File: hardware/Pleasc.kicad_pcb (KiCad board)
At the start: 4 copper layers, 60 x 60 mm, 96 parts, among them J1 2601-1104, J3 ESQ-110-14-G-D, J4 2601-1104, J5 XT30PW-M, Q1 AO3400A, Q10 AO3400A, Q11 AO3400A, Q12 AO3400A, Q13 AO3400A, Q14 AO3400A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

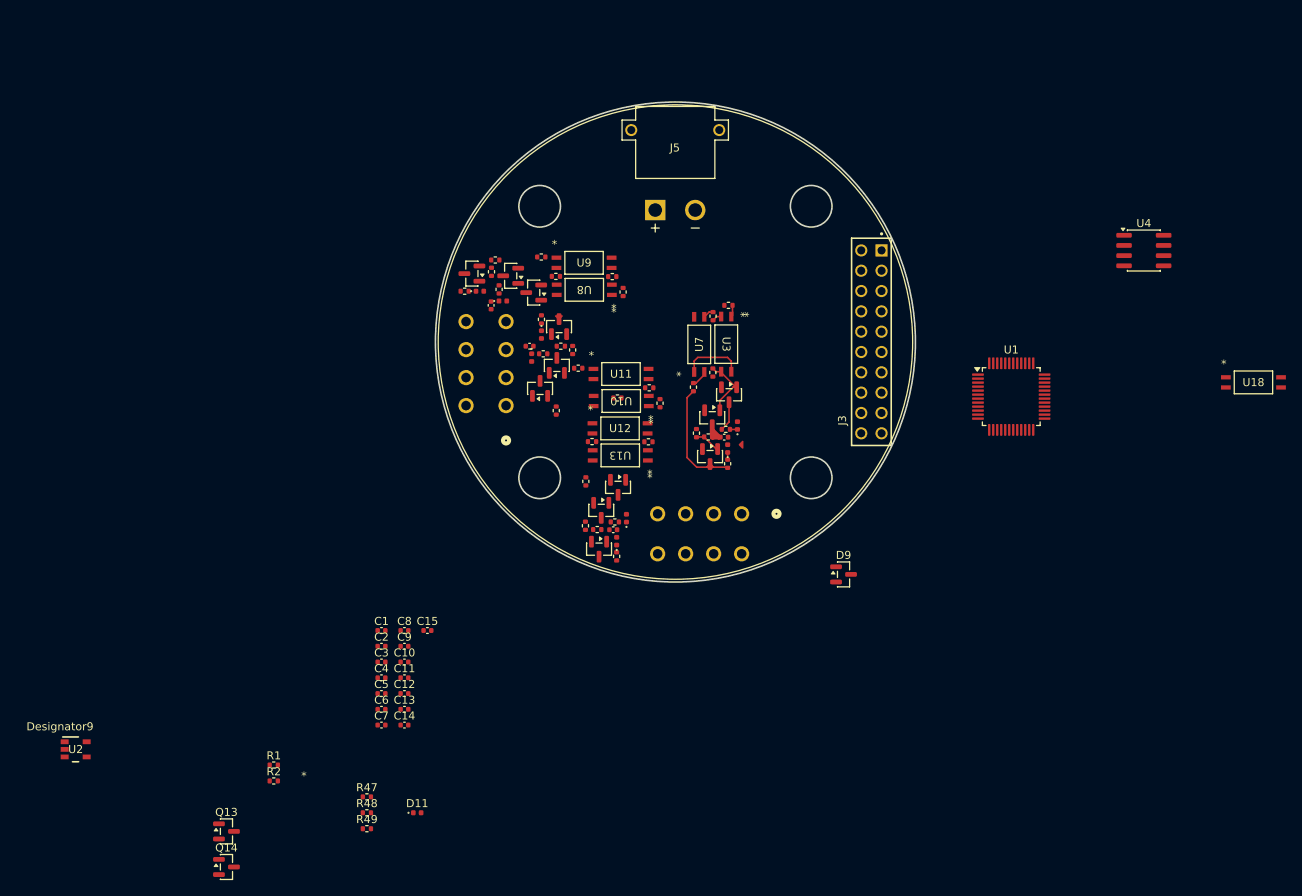
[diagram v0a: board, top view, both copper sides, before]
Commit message: Schematic complete, components layed out on the PCB
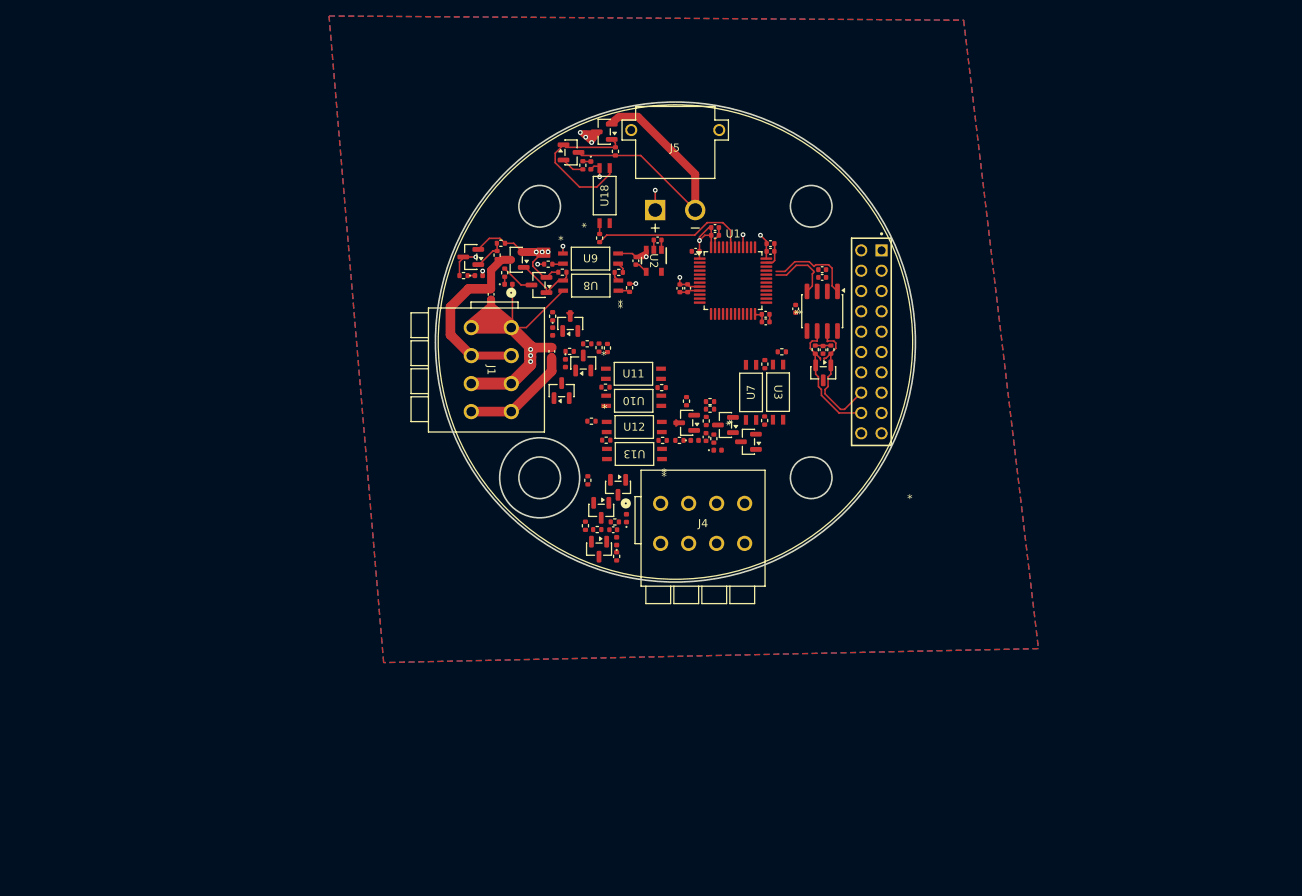
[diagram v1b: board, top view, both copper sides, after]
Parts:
- J1, J4: moved to F.Cu
- moved Q14 103.3 mm to (180.6, 60.5), turned to 180 degrees
- moved Q13 95.2 mm to (176.4, 63.0)
- moved U2 94.6 mm to (186.8, 76.6), turned to -90 degrees
- moved R48 88.3 mm to (181.9, 62.9), turned to -90 degrees
- moved R2 88.1 mm to (208.9, 87.7), turned to 90 degrees
- moved R49 87.2 mm to (177.9, 64.6), turned to 90 degrees
- moved R1 85.3 mm to (206.9, 87.7), turned to -90 degrees
- moved U18 84.4 mm to (180.6, 68.4), turned to 90 degrees
- moved D11 83.8 mm to (178.9, 64.7), turned to -90 degrees
- moved R47 75.7 mm to (180.0, 73.7), turned to 90 degrees
- moved C13 75.1 mm to (207.8, 78.7)
- moved C12 74.4 mm to (207.8, 77.7)
- moved C14 71.4 mm to (204.5, 82.6), turned to 90 degrees
- moved C3 67.7 mm to (194.4, 73.4)
- moved C9 67.3 mm to (201.3, 75.4)
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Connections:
- D11 pad 1: Net-(D11-K) -> unconnected-(D11-K-Pad1)
- J1 pad 3: /Aux1 neg -> /Main neg
- J1 pad 4: /Aux1 neg -> /Main neg
- J1 pad 7: /Aux2 neg -> /Aux1 neg
- J1 pad 8: /Aux2 neg -> /Aux1 neg
- J4 pad 7: /Main neg -> /Aux2 neg
- J4 pad 8: /Main neg -> /Aux2 neg
- Q1 pad 1: /Drogue neg -> Net-(Q1-G)
- Q10 pad 1: /Aux2 neg -> Net-(Q10-G)
- Q11 pad 1: /Aux2 neg -> Net-(Q10-G)
- Q13 pad 1: Net-(D11-K) -> Net-(Q13-G)
- Q14 pad 1: Net-(D11-K) -> Net-(Q13-G)
- Q2 pad 1: /Drogue neg -> Net-(Q1-G)
- Q4 pad 1: /Main neg -> Net-(Q4-G)
- Q5 pad 1: /Main neg -> Net-(Q4-G)
- Q7 pad 1: /Aux1 neg -> Net-(Q7-G)
- Q8 pad 1: /Aux1 neg -> Net-(Q7-G)
- R16 pad 1: /Main neg -> Net-(Q4-G)
- R25 pad 1: /Aux1 neg -> Net-(Q7-G)
- R34 pad 1: /Aux2 neg -> Net-(Q10-G)
- R48 pad 1: Net-(D11-K) -> Net-(Q13-G)
- R49 pad 2: Net-(D11-K) -> unconnected-(D11-K-Pad1)
- R6 pad 1: /Drogue neg -> Net-(Q1-G)
- U10 pad 3: /Aux1 neg -> Net-(Q7-G)
- U12 pad 3: /Aux2 neg -> Net-(Q10-G)
- U18 pad 3: Net-(D11-K) -> Net-(Q13-G)
- U3 pad 3: /Drogue neg -> Net-(Q1-G)
- U8 pad 3: /Main neg -> Net-(Q4-G)
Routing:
- net VBAT_AUX1: track 7.71 -> 95.3 mm, vias 0 -> 7
- net Net-(Q13-D): track 0.00 -> 34.5 mm
- net PGND: track 0.00 -> 34.2 mm, vias 0 -> 6
- net /Main neg: track 0.00 -> 23.5 mm
- net 3.3V: track 0.00 -> 21.2 mm, vias 0 -> 3
- net Net-(Q13-G): track 0.00 -> 20.4 mm
- net PYRO_ON: track 0.00 -> 19.5 mm
- net MAIN_FIRE: track 0.00 -> 18.3 mm, vias 0 -> 2
- net CAN_o+: track 0.00 -> 16.9 mm
- net CAN_o-: track 0.00 -> 16.3 mm
- net Net-(Q3-D): track 14.5 -> 0.00 mm
- net /Aux1 neg: track 0.00 -> 13.8 mm
- net GND: track 1.20 -> 14.5 mm, vias 0 -> 1
- net Net-(Q6-D): track 0.00 -> 12.9 mm, vias 0 -> 2
- net /Drogue neg: track 12.2 -> 0.00 mm
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- added copper zone on B.Cu, net GND
- added copper zone on F.Cu, net GND
- added copper zone on In1.Cu, net GND
- added copper zone on In2.Cu, net GND
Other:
- outline, holes or cut-outs redrawn

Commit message: All 4 Pyros circuits routed
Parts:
- moved R33 9.90 mm to (187.6, 101.5), turned to 180 degrees
- moved R34 9.16 mm to (178.7, 99.1), turned to 180 degrees
- moved R13 8.59 mm to (201.6, 97.6), turned to -90 degrees
- moved R32 4.94 mm to (185.7, 99.1), turned to 0 degrees
- moved U13 3.98 mm to (182.2, 97.4), turned to 0 degrees
- moved U12 3.96 mm to (182.2, 100.7), turned to 180 degrees
- moved C30 3.32 mm to (192.8, 101.9), turned to 0 degrees
- moved R27 3.00 mm to (175.1, 90.7), turned to 90 degrees
- moved R10 2.35 mm to (193.0, 97.3), turned to -90 degrees
- moved R9 2.21 mm to (193.4, 98.8), turned to 0 degrees
- moved R12 2.16 mm to (202.7, 88.8)
- moved R5 2.16 mm to (204.8, 87.2)
- moved R6 2.16 mm to (202.6, 95.8)
- moved U3 2.16 mm to (204.3, 92.3)
- moved U7 2.16 mm to (200.9, 92.3)
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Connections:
- J4 pad 3: /Drogue neg -> /Aux2 neg
- J4 pad 4: /Drogue neg -> /Aux2 neg
- J4 pad 7: /Aux2 neg -> /Drogue neg
- J4 pad 8: /Aux2 neg -> /Drogue neg
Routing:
- net PGND: track 34.2 -> 135.2 mm, vias 6 -> 17
- net VBAT_AUX1: track 95.3 -> 180.9 mm, vias 7 -> 12
- net AUX2_FIRE: track 0.00 -> 41.1 mm, vias 0 -> 2
- net MAIN_SEAT: track 1.34 -> 32.8 mm, vias 0 -> 2
- net AUX2_SEAT: track 0.00 -> 26.8 mm, vias 0 -> 2
- net AUX1_SEAT: track 0.00 -> 22.7 mm, vias 0 -> 2
- net AUX1_FIRE: track 0.00 -> 22.1 mm, vias 0 -> 2
- net /Aux2 neg: track 0.00 -> 22.0 mm
- net /Drogue neg: track 0.00 -> 18.0 mm
- net Net-(Q3-D): track 0.00 -> 16.5 mm, vias 0 -> 2
- net DROGUE_FIRE: track 0.00 -> 16.0 mm, vias 0 -> 2
- net Net-(Q12-D): track 0.00 -> 14.3 mm
- net Net-(Q7-G): track 0.00 -> 12.9 mm
- net Net-(Q1-G): track 0.00 -> 12.8 mm
- net Net-(Q10-G): track 0.00 -> 11.9 mm
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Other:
- outline, holes or cut-outs redrawn
